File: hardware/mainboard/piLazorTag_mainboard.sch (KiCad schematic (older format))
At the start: 11 parts, among them M1 LOGIC_LEVEL_CONVERTER

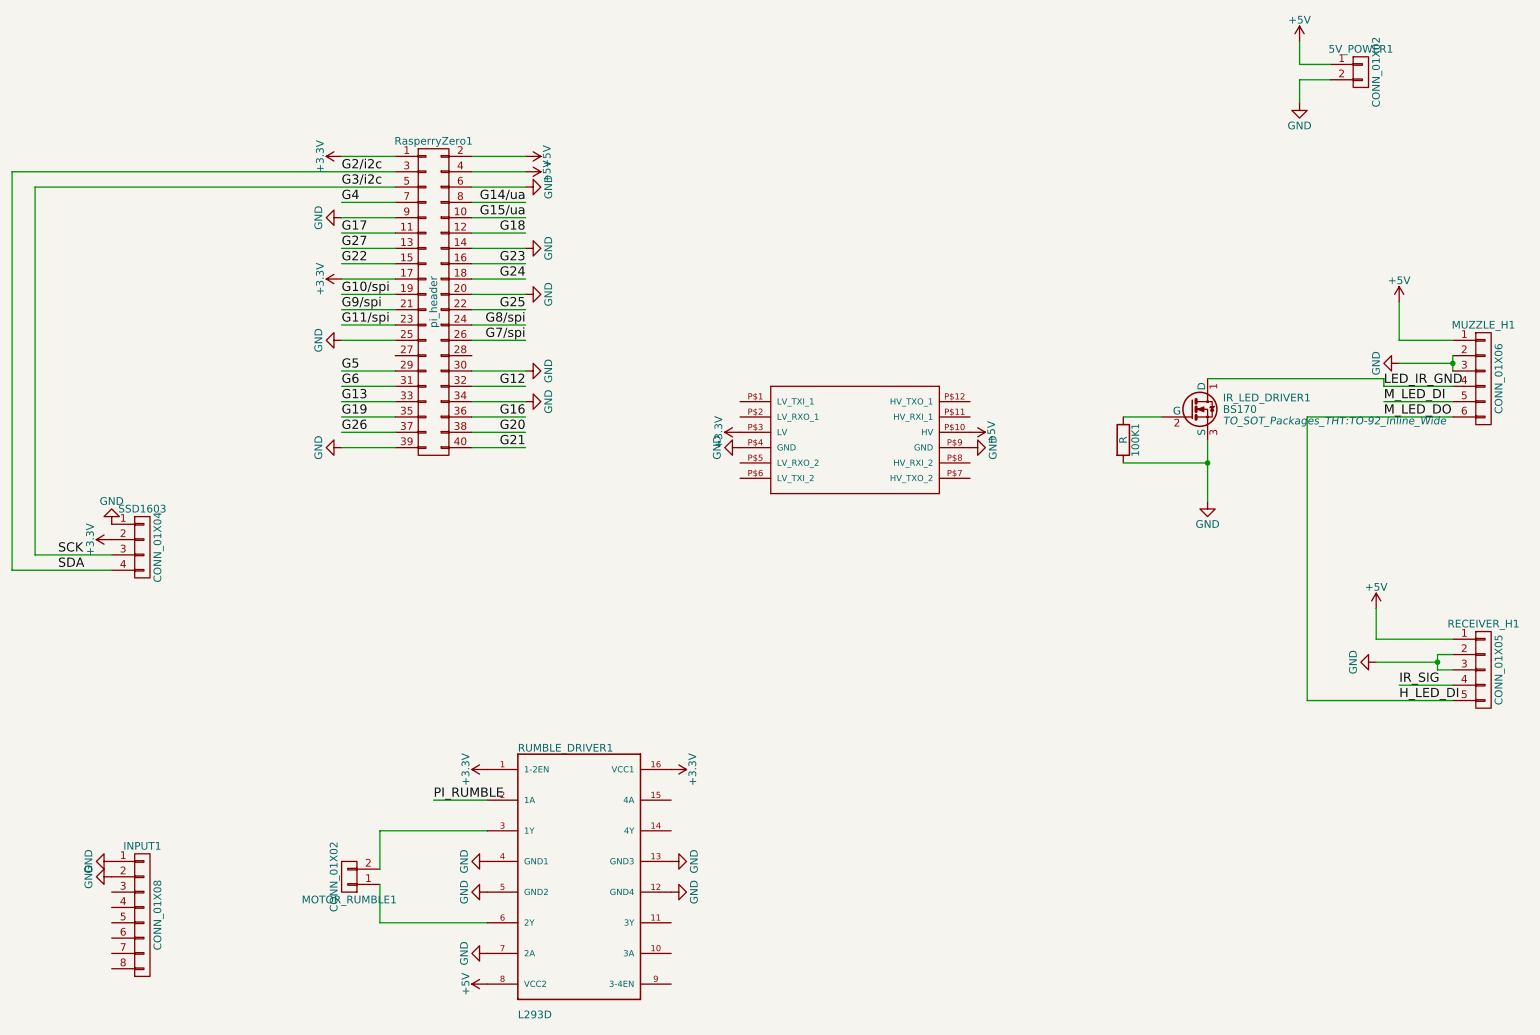
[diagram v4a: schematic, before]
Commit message: #9 Reasigned some pins to get a better board layout
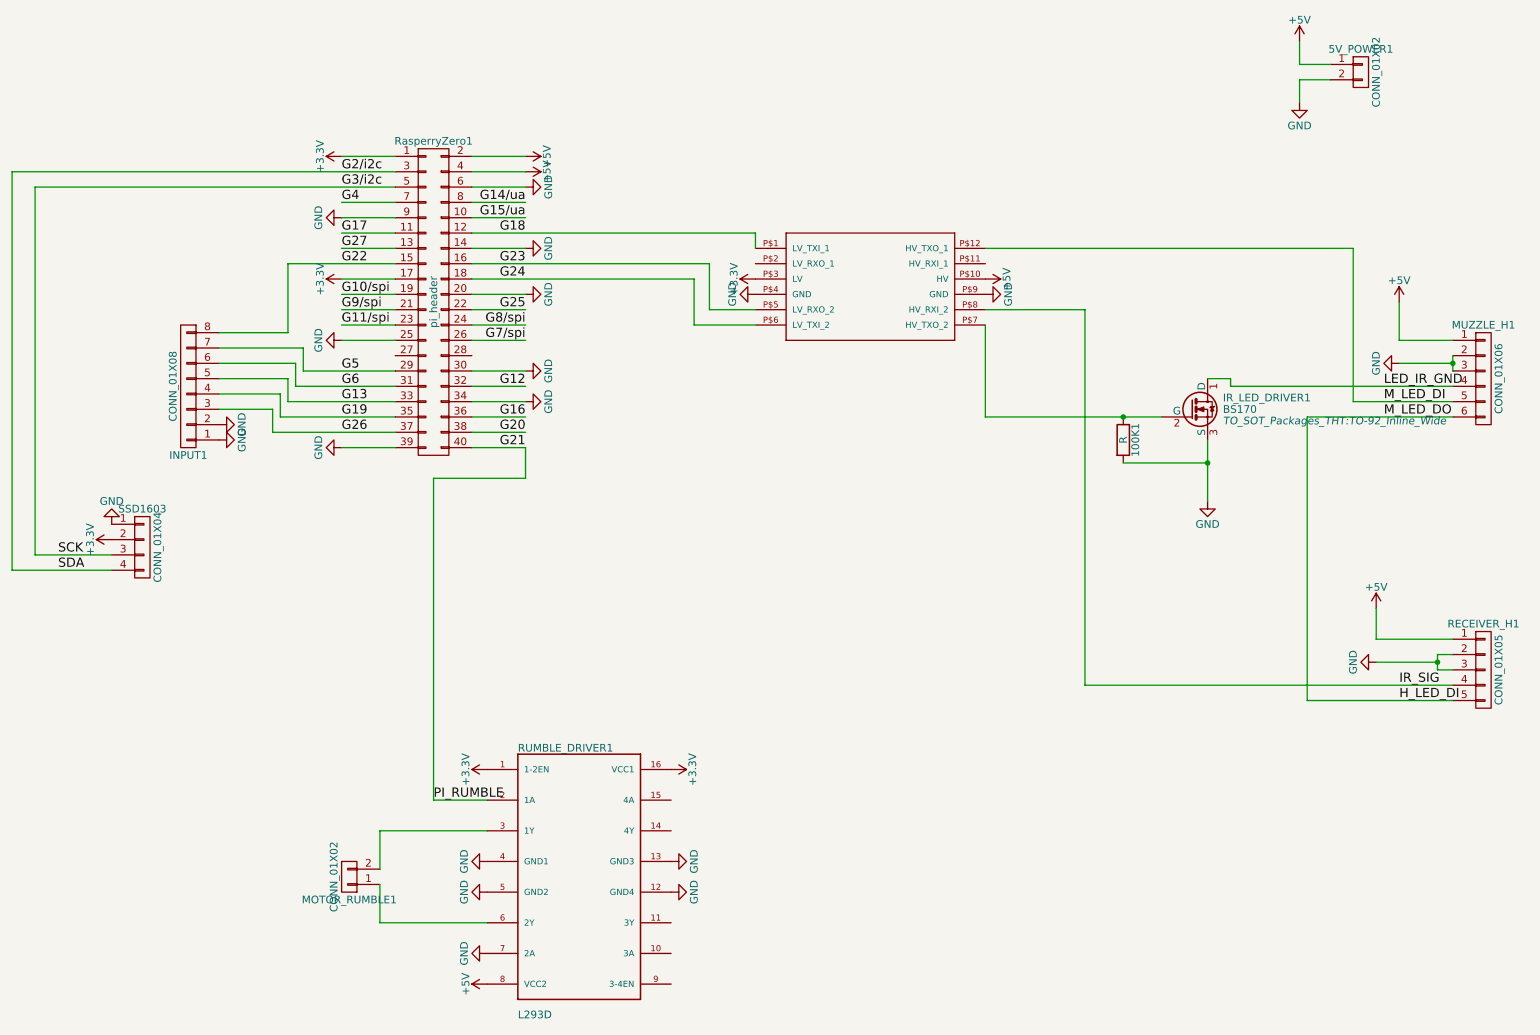
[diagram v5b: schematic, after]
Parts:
- MUZZLE_H1: footprint Pin_Headers:Pin_Header_Straight_1x06 -> Pin_Headers:Pin_Header_Straight_1x06_Pitch2.54mm
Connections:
- net PI_RUMBLE is gone; now on net G21: RUMBLE_DRIVER1.2 (1A)
- net G13: now also INPUT1.5 (P5)
- net G18: now also M1.P$1 (LV_TXI_1)
- net G19: now also INPUT1.4 (P4)
- net G22: now also INPUT1.8 (P8)
- net G23: now also M1.P$5 (LV_RXO_2)
- net G24: now also M1.P$6 (LV_TXI_2)
- net G26: now also INPUT1.3 (P3)
- net G5: now also INPUT1.7 (P7)
- net G6: now also INPUT1.6 (P6)
- net IR_SIG: now also M1.P$8 (HV_RXI_2)
- net M_LED_DI: now also M1.P$12 (HV_TXO_1)
- net at 100K1.1, IR_LED_DRIVER1.2 (G): now also M1.P$7 (HV_TXO_2)
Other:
- moved on the sheet: INPUT1

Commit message: #9 Further Progress on the mainboard
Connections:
- net G11/spi: now also INPUT1.8 (P8)
- net G22: no longer INPUT1.8 (P8)
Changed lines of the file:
@@
 	3550 2300 3200 2300
-Wire Wire Line
-	2850 2400 3550 2400
 Wire Wire Line
 	3550 2500 3200 2500
@@
 	3550 2700 3200 2700
 Wire Wire Line
-	3550 2800 3200 2800
+	2400 2800 3550 2800
 Wire Wire Line
 	3550 2900 3200 2900
@@
 	2950 2950 2950 3100
 Wire Wire Line
-	2400 2850 2850 2850
-Wire Wire Line
-	2850 2850 2850 2400
-Wire Wire Line
 	5500 2500 5500 2800
 Wire Wire Line
@@
 Wire Wire Line
 	9000 3150 8850 3150
+Wire Wire Line
+	3200 2400 3550 2400
+Wire Wire Line
+	2400 2800 2400 2850
 $EndSCHEMATC

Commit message: #9 first Mainbaordlayout done
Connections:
- net G23: now also M1.P$2 (LV_RXO_1); no longer M1.P$5 (LV_RXO_2)
- net G24: now also M1.P$5 (LV_RXO_2); no longer M1.P$6 (LV_TXI_2)
- net IR_SIG: now also M1.P$11 (HV_RXI_1); no longer M1.P$8 (HV_RXI_2)
- net at 100K1.1, IR_LED_DRIVER1.2 (G): now also M1.P$8 (HV_RXI_2); no longer M1.P$7 (HV_TXO_2)
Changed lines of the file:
@@
 	0    -1   -1   0
 $EndComp
-Wire Wire Line
-	1050 1800 3550 1800
-Wire Wire Line
-	1200 1900 3550 1900
-Wire Wire Line
-	3550 2000 3200 2000
-Wire Wire Line
-	3550 2100 3200 2100
-Wire Wire Line
-	3550 2200 3200 2200
-Wire Wire Line
-	3550 2300 3200 2300
-Wire Wire Line
-	3550 2500 3200 2500
-Wire Wire Line
-	3550 2600 3200 2600
-Wire Wire Line
-	3550 2700 3200 2700
-Wire Wire Line
-	2400 2800 3550 2800
-Wire Wire Line
-	3550 2900 3200 2900
-Wire Wire Line
-	2950 3100 3550 3100
-Wire Wire Line
-	2900 3200 3550 3200
-Wire Wire Line
-	2850 3300 3550 3300
-Wire Wire Line
-	2800 3400 3550 3400
-Wire Wire Line
-	2750 3500 3550 3500
-Wire Wire Line
-	3550 3600 3200 3600
-Wire Wire Line
-	3550 1700 3200 1700
-Wire Wire Line
-	4050 1700 4400 1700
-Wire Wire Line
-	4050 1800 4400 1800
-Wire Wire Line
-	4050 1900 4400 1900
-Wire Wire Line
-	4050 2000 4400 2000
-Wire Wire Line
-	4050 2100 4400 2100
-Wire Wire Line
-	4050 2300 4400 2300
-Wire Wire Line
-	4050 2400 5600 2400
-Wire Wire Line
-	4050 2500 5500 2500
-Wire Wire Line
-	4050 2600 4400 2600
-Wire Wire Line
-	4050 2700 4400 2700
-Wire Wire Line
-	4050 2900 4400 2900
-Wire Wire Line
-	4050 3100 4400 3100
-Wire Wire Line
-	4050 3200 4400 3200
-Wire Wire Line
-	4050 3300 4400 3300
-Wire Wire Line
-	4050 3500 4400 3500
-Wire Wire Line
-	4050 3600 4400 3600
-Wire Wire Line
-	4050 2800 4400 2800
-Wire Wire Line
-	4050 3400 4400 3400
-Wire Wire Line
-	10450 2900 10100 2900
-Wire Wire Line
-	10100 2900 10100 2650
-Wire Wire Line
-	10450 3000 10450 3100
-Wire Wire Line
-	10450 3050 10100 3050
-Connection ~ 10450 3050
-Wire Wire Line
-	9000 3200 10450 3200
-Wire Wire Line
-	9800 3300 10450 3300
-Wire Wire Line
-	9500 3400 10450 3400
-Wire Wire Line
-	9650 1100 9450 1100
-Wire Wire Line
-	9450 1100 9450 950
-Wire Wire Line
-	9650 1200 9450 1200
-Wire Wire Line
-	9450 1200 9450 1350
-Wire Wire Line
-	10450 4850 9950 4850
-Wire Wire Line
-	9950 4850 9950 4650
-Wire Wire Line
-	10450 4950 10350 4950
-Wire Wire Line
-	10350 4950 10350 5050
-Wire Wire Line
-	10350 5050 10450 5050
-Wire Wire Line
-	10350 5000 9950 5000
-Connection ~ 10350 5000
-Wire Wire Line
-	8050 5150 10450 5150
-Wire Wire Line
-	9500 5250 10450 5250
-Wire Wire Line
-	8850 3550 8850 3950
-Wire Wire Line
-	8300 3700 8850 3700
-Connection ~ 8850 3700
-Wire Wire Line
-	7400 3400 8550 3400
-Wire Wire Line
-	9500 3400 9500 5250
-Wire Wire Line
-	4150 5900 3800 5900
-Wire Wire Line
-	3450 6350 3450 6100
-Wire Wire Line
-	3450 6100 4150 6100
-Wire Wire Line
-	3450 6450 3450 6700
-Wire Wire Line
-	3450 6700 4150 6700
-Wire Wire Line
-	1200 4300 1700 4300
-Wire Wire Line
-	1050 4400 1700 4400
-Wire Wire Line
-	1050 4400 1050 1800
-Wire Wire Line
-	1200 1900 1200 4300
-Wire Wire Line
-	2400 3350 2750 3350
-Wire Wire Line
-	2750 3350 2750 3500
-Wire Wire Line
-	2400 3250 2800 3250
-Wire Wire Line
-	2800 3250 2800 3400
-Wire Wire Line
-	2400 3150 2850 3150
-Wire Wire Line
-	2850 3150 2850 3300
-Wire Wire Line
-	2400 3050 2900 3050
-Wire Wire Line
-	2900 3050 2900 3200
-Wire Wire Line
-	2400 2950 2950 2950
-Wire Wire Line
-	2950 2950 2950 3100
-Wire Wire Line
-	5500 2500 5500 2800
-Wire Wire Line
-	5500 2800 5900 2800
-Wire Wire Line
-	5600 2400 5600 2700
-Wire Wire Line
-	5600 2700 5900 2700
-Wire Wire Line
-	5900 2200 5900 2300
-Wire Wire Line
-	4050 2200 5900 2200
 $Comp
 L LOGIC_LEVEL_CONVERTER M1
@@
 $EndComp
 Wire Wire Line
+	1050 1800 3550 1800
+Wire Wire Line
+	1200 1900 3550 1900
+Wire Wire Line
+	3550 2000 3200 2000
+Wire Wire Line
+	3550 2100 3200 2100
+Wire Wire Line
+	3550 2200 3200 2200
+Wire Wire Line
+	3550 2300 3200 2300
+Wire Wire Line
+	3550 2500 3200 2500
+Wire Wire Line
+	3550 2600 3200 2600
+Wire Wire Line
+	3550 2700 3200 2700
+Wire Wire Line
+	2400 2800 3550 2800
+Wire Wire Line
+	3550 2900 3200 2900
+Wire Wire Line
+	2950 3100 3550 3100
+Wire Wire Line
+	2900 3200 3550 3200
+Wire Wire Line
+	2850 3300 3550 3300
+Wire Wire Line
+	2800 3400 3550 3400
+Wire Wire Line
+	2750 3500 3550 3500
+Wire Wire Line
+	3550 3600 3200 3600
+Wire Wire Line
+	3550 1700 3200 1700
+Wire Wire Line
+	4050 1700 4400 1700
+Wire Wire Line
+	4050 1800 4400 1800
+Wire Wire Line
+	4050 1900 4400 1900
+Wire Wire Line
+	4050 2000 4400 2000
+Wire Wire Line
+	4050 2100 4400 2100
+Wire Wire Line
+	4050 2300 4400 2300
+Wire Wire Line
+	4050 2600 4400 2600
+Wire Wire Line
+	4050 2700 4400 2700
+Wire Wire Line
+	4050 2900 4400 2900
+Wire Wire Line
+	4050 3100 4400 3100
+Wire Wire Line
+	4050 3200 4400 3200
+Wire Wire Line
+	4050 3300 4400 3300
+Wire Wire Line
+	4050 3500 4400 3500
+Wire Wire Line
+	4050 3600 4400 3600
+Wire Wire Line
+	4050 2800 4400 2800
+Wire Wire Line
+	4050 3400 4400 3400
+Wire Wire Line
+	10450 2900 10100 2900
+Wire Wire Line
+	10100 2900 10100 2650
+Wire Wire Line
+	10450 3000 10450 3100
+Wire Wire Line
+	10450 3050 10100 3050
+Connection ~ 10450 3050
+Wire Wire Line
+	9000 3200 10450 3200
+Wire Wire Line
+	9800 3300 10450 3300
+Wire Wire Line
+	9500 3400 10450 3400
+Wire Wire Line
+	9650 1100 9450 1100
+Wire Wire Line
+	9450 1100 9450 950
+Wire Wire Line
+	9650 1200 9450 1200
+Wire Wire Line
+	9450 1200 9450 1350
+Wire Wire Line
+	10450 4850 9950 4850
+Wire Wire Line
+	9950 4850 9950 4650
+Wire Wire Line
+	10450 4950 10350 4950
+Wire Wire Line
+	10350 4950 10350 5050
+Wire Wire Line
+	10350 5050 10450 5050
+Wire Wire Line
+	10350 5000 9950 5000
+Connection ~ 10350 5000
+Wire Wire Line
+	8050 5150 10450 5150
+Wire Wire Line
+	9500 5250 10450 5250
+Wire Wire Line
+	8850 3550 8850 3950
+Wire Wire Line
+	8300 3700 8850 3700
+Connection ~ 8850 3700
+Wire Wire Line
+	9500 3400 9500 5250
+Wire Wire Line
+	4150 5900 3800 5900
+Wire Wire Line
+	3450 6350 3450 6100
+Wire Wire Line
+	3450 6100 4150 6100
+Wire Wire Line
+	3450 6450 3450 6700
+Wire Wire Line
+	3450 6700 4150 6700
+Wire Wire Line
+	1200 4300 1700 4300
+Wire Wire Line
+	1050 4400 1700 4400
+Wire Wire Line
+	1050 4400 1050 1800
+Wire Wire Line
+	1200 1900 1200 4300
+Wire Wire Line
+	2400 3350 2750 3350
+Wire Wire Line
+	2750 3350 2750 3500
+Wire Wire Line
+	2400 3250 2800 3250
+Wire Wire Line
+	2800 3250 2800 3400
+Wire Wire Line
+	2400 3150 2850 3150
+Wire Wire Line
+	2850 3150 2850 3300
+Wire Wire Line
+	2400 3050 2900 3050
+Wire Wire Line
+	2900 3050 2900 3200
+Wire Wire Line
+	2400 2950 2950 2950
+Wire Wire Line
+	2950 2950 2950 3100
+Wire Wire Line
+	5900 2200 5900 2300
+Wire Wire Line
+	4050 2200 5900 2200
+Wire Wire Line
 	7400 2300 9800 2300
 Wire Wire Line
 	9800 2300 9800 3300
-Wire Wire Line
-	7400 2800 7400 3400
 Connection ~ 8300 3400
 Wire Wire Line
-	7400 2700 8050 2700
-Wire Wire Line
-	8050 2700 8050 5150
-Wire Wire Line
 	3800 5900 3800 3800
 Wire Wire Line
@@
 Wire Wire Line
 	2400 2800 2400 2850
+Wire Wire Line
+	4050 2400 5900 2400
+Wire Wire Line
+	8050 2400 8050 5150
+Wire Wire Line
+	7400 2400 8050 2400
+Wire Wire Line
+	4050 2500 5500 2500
+Wire Wire Line
+	5900 2700 5500 2700
+Wire Wire Line
+	5500 2700 5500 2500
+Wire Wire Line
+	8550 3400 7600 3400
+Wire Wire Line
+	7600 3400 7600 2700
+Wire Wire Line
+	7600 2700 7400 2700
 $EndSCHEMATC
